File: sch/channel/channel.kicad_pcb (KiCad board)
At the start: 2 copper layers, 100 x 100 mm, 98 parts, among them IC1 STM32F030F4, IC10 74HCT125, IC2 L200, IC3 TL072, IC4 LM2594, IC5 TL074, IC6 LM2594, IC8 MCP1700-3002E/TT, IC9 MCP1824ST-3302E, P1 CONN_2, P10 CONN_3, P11 CONN_6, P12 CONN_1, P13 CONN_2, P14 CONN_1, P15 CONN_1, P16 CONN_1, P17 CONN_1, P18 CONN_1, P19 CONN_5, P2 CONN_3, P3 DC_JACK, P4 CONN_1, P5 CONN_1, P6 CONN_3, P7 CONN_5, P8 CONN_1, P9 CONN_1, Q1 BC817, SW1 SWITCH_INV_MECH, SW2 DUAL_SWITCH_INV

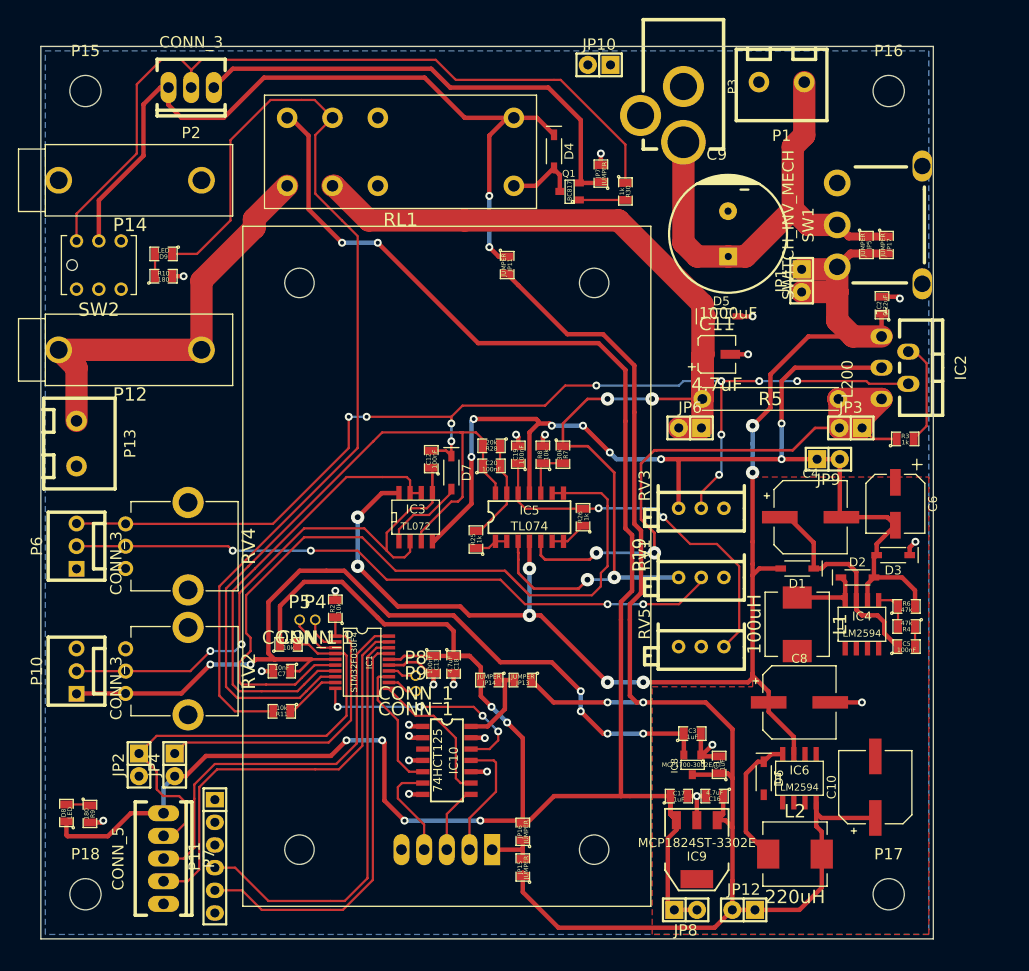
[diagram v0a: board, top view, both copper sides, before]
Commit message: A few tweaks to improve the layout.  Still not sorted silk screen.
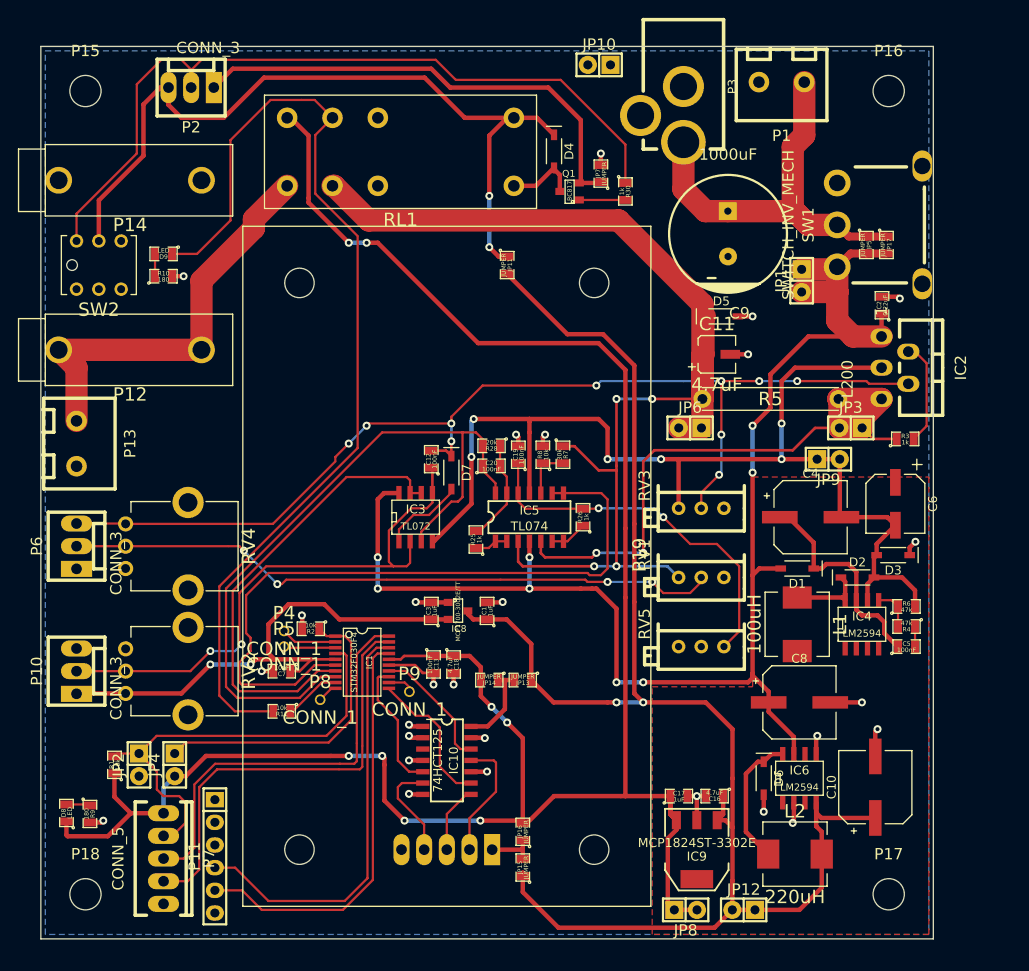
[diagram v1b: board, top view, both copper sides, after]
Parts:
- P2: footprint Sockets_MOLEX_KK-System:Socket_MOLEX-KK-RM2-54mm_Lock_3pin_straight -> Nathan_THT:MOLEX_KK_3
- moved C3 32.3 mm to (143.8, 113.2), turned to 90 degrees
- moved IC8 31.4 mm to (146.8, 113.2), turned to 270 degrees
- moved C1 31.2 mm to (150.0, 113.2)
- moved R1 23.7 mm to (108.2, 130.5), turned to 90 degrees
- moved P8 11.0 mm to (131.3, 123.2)
- moved P4 3.72 mm to (127.2, 115.5)
- moved R2 3.55 mm to (130.2, 115.2), turned to 180 degrees
- moved P5 3.47 mm to (127.2, 117.2)
- moved P9 0.70 mm to (141.3, 122.3)
- turned C9 to 180 degrees
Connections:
- IC1 pad 10: /LOAD -> Net-(IC1-Pad10)
- IC1 pad 14: Net-(IC1-Pad14) -> /LOAD
- IC10 pad 3: (no net) -> Net-(IC10-Pad3)
- P11 pad 3: (no net) -> Net-(P11-Pad3)
- P11 pad 6: (no net) -> Net-(P11-Pad6)
- P15 pad 1: (no net) -> Net-(P15-Pad1)
- P16 pad 1: (no net) -> Net-(P16-Pad1)
- P17 pad 1: (no net) -> Net-(P17-Pad1)
- P18 pad 1: (no net) -> Net-(P18-Pad1)
- P3 pad 3: (no net) -> Net-(P3-Pad3)
- P8 pad 1: Net-(IC1-Pad14) -> Net-(IC1-Pad10)
- RL1 pad 1NC: (no net) -> Net-(RL1-Pad1NC)
- RV1 pad 1: (no net) -> Net-(RV1-Pad1)
- RV3 pad 1: (no net) -> Net-(RV3-Pad1)
- RV4 pad 3: (no net) -> Net-(RV4-Pad3)
- RV5 pad 3: (no net) -> Net-(RV5-Pad3)
- SW1 pad 1: (no net) -> Net-(SW1-Pad1)
- SW2 pad 1: (no net) -> Net-(SW2-Pad1)
- SW2 pad 4: (no net) -> Net-(SW2-Pad4)
- SW2 pad 5: (no net) -> Net-(SW2-Pad5)
- SW2 pad 6: (no net) -> Net-(SW2-Pad6)
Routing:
- net +3.0VA: track 99.6 -> 59.6 mm, vias 6 -> 2
- net +3.3V: track 269.7 -> 238.5 mm
- net /LOAD: track 25.8 -> 14.3 mm, vias 4 -> 0
- net /VMEAS: track 88.2 -> 78.4 mm
- net GND: track 49.4 -> 58.9 mm, vias 22 -> 27
- net +5V: track 170.1 -> 176.7 mm
- net /VIN_SW: track 52.9 -> 47.5 mm
- net /OUT: track 134.6 -> 130.3 mm
- net Net-(IC1-Pad4): track 53.8 -> 50.0 mm
- net Net-(IC1-Pad14): track 3.22 -> 0.00 mm
- net -3.3V: track 122.8 -> 125.3 mm, vias 8 -> 6
- net /OUT_SENSE: track 72.9 -> 70.5 mm
- net Net-(IC1-Pad10): track 0.00 -> 2.23 mm
- net Net-(IC1-Pad2): track 4.15 -> 6.26 mm
- net Net-(C12-Pad2): track 124.1 -> 122.0 mm
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
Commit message: Started ripping up the channel board to add a heatsink for standalone mode, and switch the display around so it faces the right way.
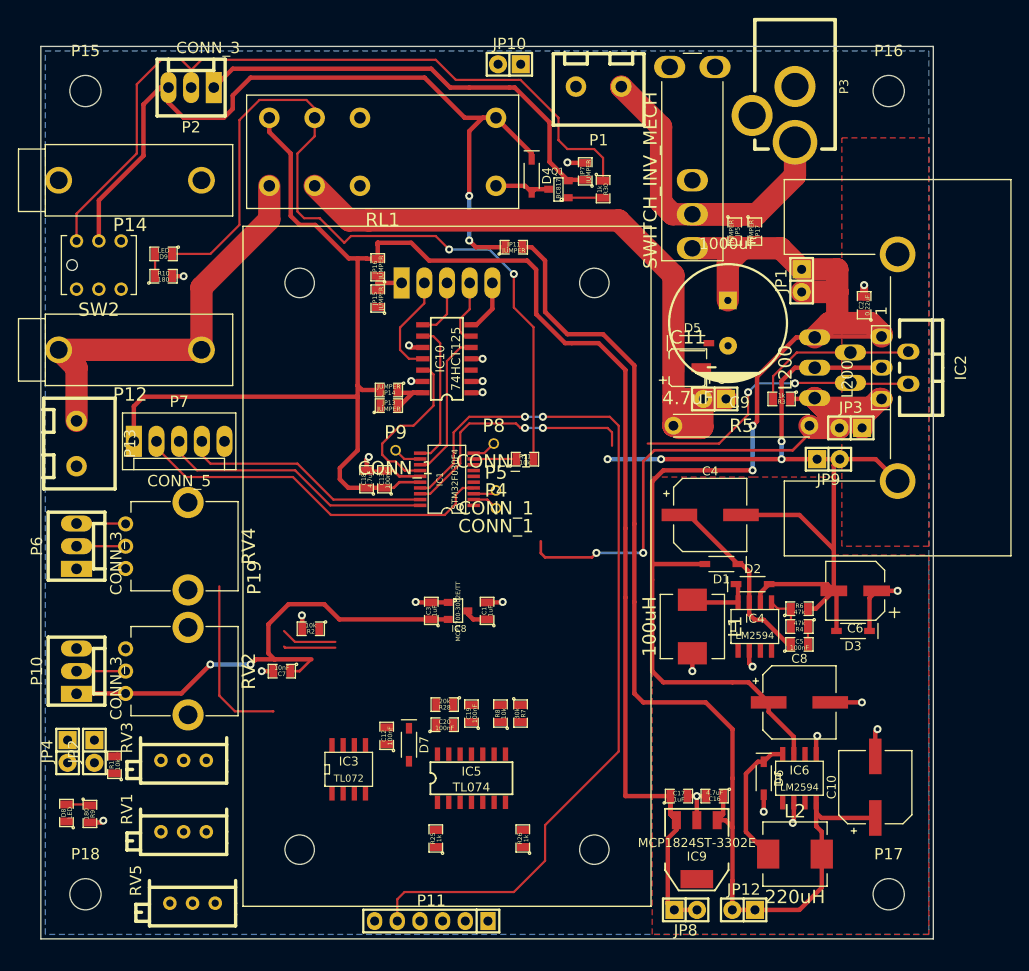
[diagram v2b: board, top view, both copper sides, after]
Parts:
- added IC7: L200, Nathan_THT:HSK_AAVID_6398BG, F.Cu at (196.0, 86.0)
- P7: footprint Sockets_MOLEX_KK-System:Socket_MOLEX-KK-RM2-54mm_Lock_5pin_straight -> Nathan_THT:MOLEX_KK_5
- SW1: footprint Nathan_THT:SW_CK_1101MxS3 -> Nathan_THT:SW_TE_GEMINI_A_RA
- moved P19 71.6 mm to (129.0, 76.5), turned to 270 degrees
- moved JP15 65.8 mm to (137.8, 78.2)
- moved JP16 65.3 mm to (137.8, 74.8)
- moved RV1 64.6 mm to (116.0, 138.0)
- moved RV3 64.5 mm to (116.0, 130.0)
- moved RV5 63.8 mm to (117.0, 146.0)
- moved P7 46.8 mm to (115.5, 94.2), turned to 0 degrees
- moved IC10 45.0 mm to (145.5, 85.0), turned to 90 degrees
- moved R11 39.3 mm to (154.2, 96.2), turned to 0 degrees
- moved R26 36.6 mm to (154.0, 138.8)
- moved P8 34.7 mm to (150.8, 94.5)
- moved JP14 34.4 mm to (139.0, 88.5)
- moved JP13 34.2 mm to (139.0, 90.2), turned to 0 degrees
- moved R25 33.8 mm to (144.2, 138.8)
- moved C12 31.4 mm to (138.8, 127.2)
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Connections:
- C9 pad 1: /VIN_SW -> +VIN
- IC10 pad 3: Net-(IC10-Pad3) -> (no net)
- P11 pad 3: Net-(P11-Pad3) -> (no net)
- P11 pad 6: Net-(P11-Pad6) -> (no net)
- P15 pad 1: Net-(P15-Pad1) -> (no net)
- P16 pad 1: Net-(P16-Pad1) -> (no net)
- P17 pad 1: Net-(P17-Pad1) -> (no net)
- P18 pad 1: Net-(P18-Pad1) -> (no net)
- P3 pad 3: Net-(P3-Pad3) -> (no net)
- RL1 pad 1NC: Net-(RL1-Pad1NC) -> (no net)
- RV1 pad 1: Net-(RV1-Pad1) -> (no net)
- RV3 pad 1: Net-(RV3-Pad1) -> (no net)
- RV4 pad 3: Net-(RV4-Pad3) -> (no net)
- RV5 pad 3: Net-(RV5-Pad3) -> (no net)
- SW1 pad 1: Net-(SW1-Pad1) -> (no net)
- SW2 pad 1: Net-(SW2-Pad1) -> (no net)
- SW2 pad 4: Net-(SW2-Pad4) -> (no net)
- SW2 pad 5: Net-(SW2-Pad5) -> (no net)
- SW2 pad 6: Net-(SW2-Pad6) -> (no net)
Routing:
- net Net-(C12-Pad2): track 122.0 -> 39.2 mm, vias 10 -> 2
- net /ICUR_MEAS: track 82.3 -> 0.00 mm
- net /VMEAS: track 78.4 -> 0.00 mm
- net Net-(P6-Pad2): track 73.6 -> 5.50 mm, vias 4 -> 0
- net Net-(C12-Pad1): track 62.9 -> 5.50 mm, vias 2 -> 0
- net Net-(IC1-Pad17): track 46.9 -> 101.0 mm, vias 0 -> 2
- net /ISET_MEAS: track 51.2 -> 0.00 mm
- net +5V: track 176.7 -> 127.8 mm, vias 2 -> 0
- net /OUT: track 130.3 -> 82.4 mm, vias 4 -> 0
- net Net-(C19-Pad1): track 41.8 -> 0.00 mm, vias 2 -> 0
- net +3.3V: track 238.5 -> 202.1 mm, vias 8 -> 0
- net Net-(IC1-Pad1): track 34.2 -> 0.00 mm
- net (no net): track 0.00 -> 31.1 mm
- net -3.3V: track 125.3 -> 101.7 mm, vias 6 -> 4
- net Net-(IC1-Pad19): track 49.1 -> 28.1 mm
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- added copper zone on F.Cu, net -3.3V

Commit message: More or less happy with the channel PCB.  Needs silk screen sorting out.
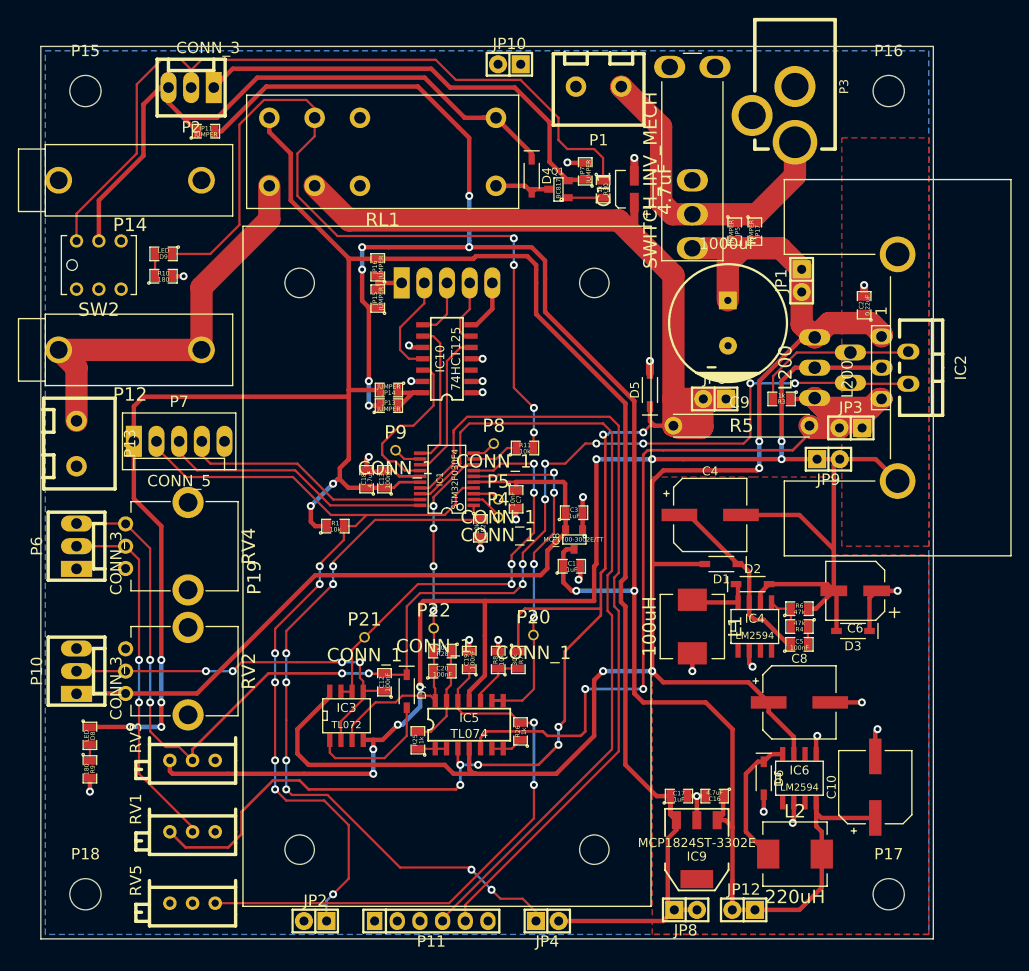
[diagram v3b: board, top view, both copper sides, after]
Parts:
- added P20: CONN_1, Nathan_THT:TEST_POINT, F.Cu at (155.2, 116.0)
- added P21: CONN_1, Nathan_THT:TEST_POINT, F.Cu at (136.3, 116.2)
- added P22: CONN_1, Nathan_THT:TEST_POINT, F.Cu at (144.0, 115.2)
- moved JP4 57.0 mm to (156.8, 148.0), turned to 180 degrees
- moved JP11 36.9 mm to (118.5, 59.5)
- moved R1 36.4 mm to (133.0, 103.8), turned to 0 degrees
- moved C7 32.6 mm to (153.2, 100.8), turned to 270 degrees
- moved JP2 31.2 mm to (130.8, 148.0), turned to 0 degrees
- moved R2 22.1 mm to (149.2, 104.0), turned to 270 degrees
- moved C11 20.9 mm to (166.5, 66.0), turned to 0 degrees
- moved C3 19.4 mm to (159.8, 102.2), turned to 0 degrees
- moved IC8 15.3 mm to (159.8, 105.2), turned to 180 degrees
- moved R26 12.0 mm to (153.8, 126.8)
- moved R25 11.2 mm to (142.2, 127.8)
- moved C1 10.7 mm to (159.5, 108.2), turned to 0 degrees
- moved D8 9.03 mm to (105.5, 127.2), turned to 270 degrees
- moved D5 7.08 mm to (168.2, 88.5), turned to 90 degrees
- moved C12 6.01 mm to (138.5, 121.2)
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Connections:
- IC10 pad 3: (no net) -> Net-(IC10-Pad3)
- P11 pad 3: (no net) -> Net-(P11-Pad3)
- P11 pad 6: (no net) -> Net-(P11-Pad6)
- P15 pad 1: (no net) -> Net-(P15-Pad1)
- P16 pad 1: (no net) -> Net-(P16-Pad1)
- P17 pad 1: (no net) -> Net-(P17-Pad1)
- P18 pad 1: (no net) -> Net-(P18-Pad1)
- P3 pad 3: (no net) -> Net-(P3-Pad3)
- RL1 pad 1NC: (no net) -> Net-(RL1-Pad1NC)
- RV1 pad 1: (no net) -> Net-(RV1-Pad1)
- RV3 pad 1: (no net) -> Net-(RV3-Pad1)
- RV4 pad 3: (no net) -> Net-(RV4-Pad3)
- RV5 pad 3: (no net) -> Net-(RV5-Pad3)
- SW1 pad 1: (no net) -> Net-(SW1-Pad1)
- SW2 pad 1: (no net) -> Net-(SW2-Pad1)
- SW2 pad 4: (no net) -> Net-(SW2-Pad4)
- SW2 pad 5: (no net) -> Net-(SW2-Pad5)
- SW2 pad 6: (no net) -> Net-(SW2-Pad6)
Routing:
- net /OUT: track 82.4 -> 204.3 mm, vias 0 -> 7
- net Net-(C12-Pad2): track 39.2 -> 149.5 mm, vias 2 -> 12
- net -3.3V: track 101.7 -> 196.6 mm, vias 4 -> 8
- net +5V: track 127.8 -> 219.6 mm, vias 0 -> 8
- net Net-(IC1-Pad1): track 0.00 -> 82.7 mm, vias 0 -> 8
- net Net-(C19-Pad1): track 0.00 -> 64.6 mm, vias 0 -> 2
- net Net-(IC1-Pad18): track 28.7 -> 90.3 mm, vias 2 -> 0
- net Net-(IC1-Pad4): track 41.7 -> 98.7 mm, vias 0 -> 7
- net +3.3V: track 202.1 -> 257.2 mm, vias 0 -> 6
- net /ISET_MEAS: track 0.00 -> 48.5 mm, vias 0 -> 4
- net +VIN: track 147.0 -> 193.9 mm, vias 2 -> 4
- net /ICUR_MEAS: track 0.00 -> 41.5 mm, vias 0 -> 4
- net /VMEAS: track 0.00 -> 41.2 mm, vias 0 -> 4
- net Net-(C12-Pad1): track 5.50 -> 44.5 mm, vias 0 -> 4
- net Net-(P6-Pad2): track 5.50 -> 40.9 mm, vias 0 -> 2
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
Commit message: Final changes before ordering PCBs
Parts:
- added Sym: Symbol_OSHW-Logo_SilkScreen_BIG_07Jul2012, Footprint_Symbols:Symbol_OSHW-Logo_SilkScreen_BIG, B.Cu at (201.8, 127.5)
- JP1: value JUMPER -> VIN
- JP10: value JUMPER -> GND
- JP12: value JUMPER -> 5V
- JP3: value JUMPER -> OUT_SENSE
- JP6: value JUMPER -> OUT
- JP8: value JUMPER -> 3.3V
- JP9: value JUMPER -> -3.3V
- P1: value CONN_2 -> 17-24VDC
- P10: value CONN_3 -> CURRENT
- P11: value CONN_6 -> FTDI
- P13: value CONN_2 -> OUTPUT
- P19: value CONN_5 -> LED_DISPLAY
- P2: value CONN_3 -> OUT_ON
- P20: value CONN_1 -> V; moved to B.Cu
- P21: value CONN_1 -> I_SET; moved to B.Cu
- P22: value CONN_1 -> I_NOW; moved to B.Cu
- P3: value DC_JACK -> 17-24VDC PIN +VE
- P6: value CONN_3 -> VOLTAGE
- P7: value CONN_5 -> SWD
- SW2: value DUAL_SWITCH_INV -> OUT_ON
- moved JP9 12.6 mm to (181.0, 106.5), turned to 270 degrees
- moved D8 3.00 mm to (105.5, 130.2)
- moved R9 3.00 mm to (105.5, 134.0)
- moved D9 1.00 mm to (114.8, 73.2)
- moved R10 1.00 mm to (114.8, 75.8)
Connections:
- IC10 pad 3: Net-(IC10-Pad3) -> (no net)
- P11 pad 3: Net-(P11-Pad3) -> (no net)
- P11 pad 6: Net-(P11-Pad6) -> (no net)
- P15 pad 1: Net-(P15-Pad1) -> (no net)
- P16 pad 1: Net-(P16-Pad1) -> (no net)
- P17 pad 1: Net-(P17-Pad1) -> (no net)
- P18 pad 1: Net-(P18-Pad1) -> (no net)
- P3 pad 3: Net-(P3-Pad3) -> (no net)
- RL1 pad 1NC: Net-(RL1-Pad1NC) -> (no net)
- RV1 pad 1: Net-(RV1-Pad1) -> (no net)
- RV3 pad 1: Net-(RV3-Pad1) -> (no net)
- RV4 pad 3: Net-(RV4-Pad3) -> (no net)
- RV5 pad 3: Net-(RV5-Pad3) -> (no net)
- SW1 pad 1: Net-(SW1-Pad1) -> (no net)
- SW2 pad 1: Net-(SW2-Pad1) -> (no net)
- SW2 pad 4: Net-(SW2-Pad4) -> (no net)
- SW2 pad 5: Net-(SW2-Pad5) -> (no net)
- SW2 pad 6: Net-(SW2-Pad6) -> (no net)
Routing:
- net -3.3V: track 196.6 -> 202.9 mm
- net GND: track 69.8 -> 75.2 mm, vias 27 -> 29
- net +3.3V: track 257.2 -> 259.2 mm
- net /OUT_ON: track 91.4 -> 90.4 mm
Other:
- board text added: "1"
- board text added: "General Purpose Bench Supply Copyright Nathan Dumont 2014 http://www.nathandumont.com/blog/bench-power-supply-design CC-BY"
- board text added: "REV A 2014-05-18"
